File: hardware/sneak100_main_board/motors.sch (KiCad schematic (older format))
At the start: 16 parts, among them J3 Conn_01x06, J4 Conn_01x06, J5 Conn_01x06, J6 Conn_01x06, U1 DRV8835, U2 DRV8835, U3 DRV8835, U4 DRV8835

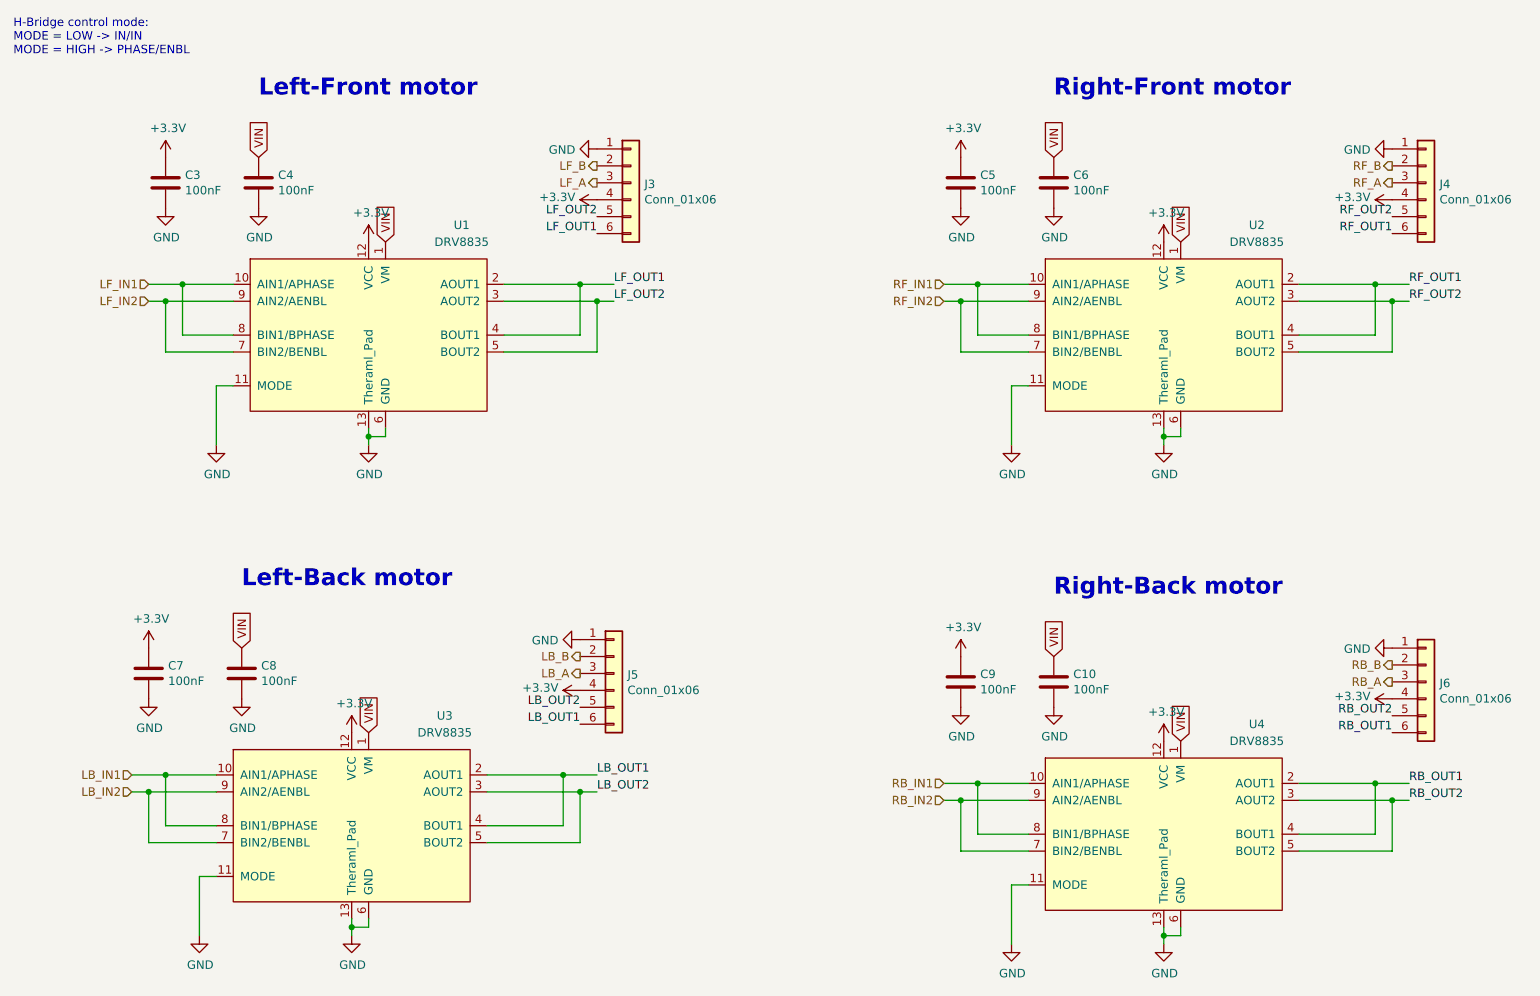
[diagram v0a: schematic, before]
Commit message: Add stm32f405 uC scheme
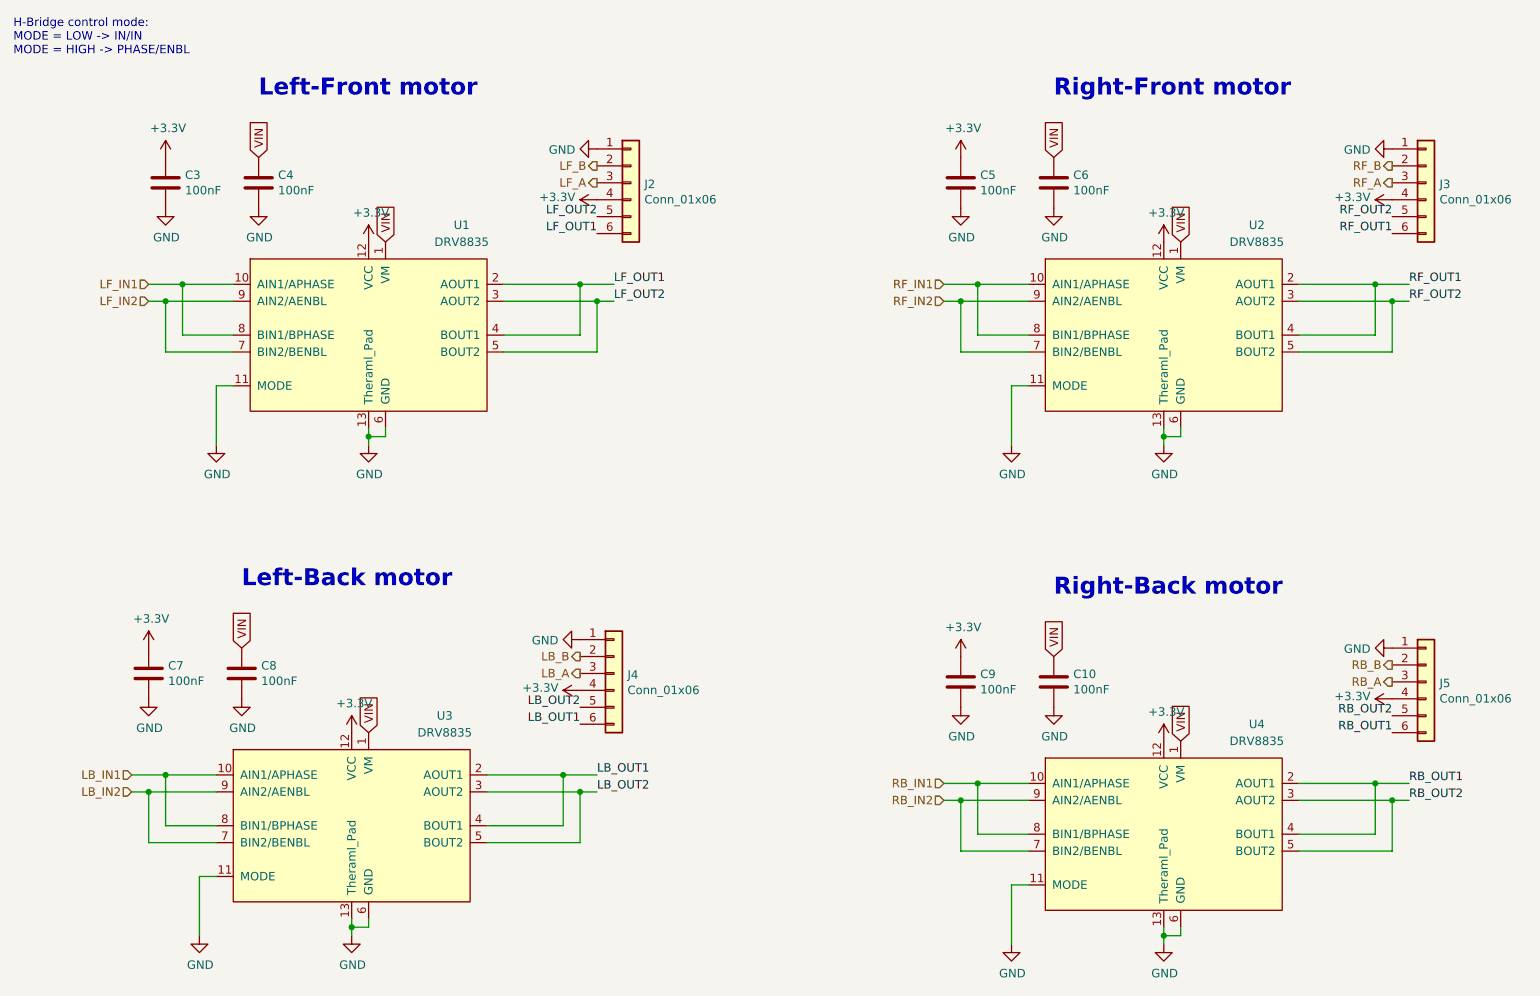
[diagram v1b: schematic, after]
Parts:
- renumbered J3 to J2, J4 to J3, J5 to J4, J6 to J5
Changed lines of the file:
@@
 $Descr A4 11693 8268
 encoding utf-8
-Sheet 4 7
+Sheet 3 7
 Title ""
 Date ""
@@
 Connection ~ 1800 2350
 $Comp
-L Connector_Generic:Conn_01x06 J3
+L Connector_Generic:Conn_01x06 J2
 U 1 1 60E9010F
 P 4550 1650
-F 0 "J3" H 4630 1642 50  0000 L CNN
+F 0 "J2" H 4630 1642 50  0000 L CNN
 F 1 "Conn_01x06" H 4630 1551 50  0000 L CNN
 F 2 "Connector_PinHeader_2.54mm:PinHeader_1x06_P2.54mm_Vertical" H 4550 1650 50  0001 C CNN
@@
 Connection ~ 6500 2350
 $Comp
-L Connector_Generic:Conn_01x06 J4
+L Connector_Generic:Conn_01x06 J3
 U 1 1 60EAF600
 P 9250 1650
-F 0 "J4" H 9330 1642 50  0000 L CNN
+F 0 "J3" H 9330 1642 50  0000 L CNN
 F 1 "Conn_01x06" H 9330 1551 50  0000 L CNN
 F 2 "Connector_PinHeader_2.54mm:PinHeader_1x06_P2.54mm_Vertical" H 9250 1650 50  0001 C CNN
@@
 Connection ~ 1700 5250
 $Comp
-L Connector_Generic:Conn_01x06 J5
+L Connector_Generic:Conn_01x06 J4
 U 1 1 60EB4F56
 P 4450 4550
-F 0 "J5" H 4530 4542 50  0000 L CNN
+F 0 "J4" H 4530 4542 50  0000 L CNN
 F 1 "Conn_01x06" H 4530 4451 50  0000 L CNN
 F 2 "Connector_PinHeader_2.54mm:PinHeader_1x06_P2.54mm_Vertical" H 4450 4550 50  0001 C CNN
@@
 Connection ~ 6500 5300
 $Comp
-L Connector_Generic:Conn_01x06 J6
+L Connector_Generic:Conn_01x06 J5
 U 1 1 60EC1868
 P 9250 4600
-F 0 "J6" H 9330 4592 50  0000 L CNN
+F 0 "J5" H 9330 4592 50  0000 L CNN
 F 1 "Conn_01x06" H 9330 4501 50  0000 L CNN
 F 2 "Connector_PinHeader_2.54mm:PinHeader_1x06_P2.54mm_Vertical" H 9250 4600 50  0001 C CNN

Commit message: Hardware configuration schematic
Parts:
- renumbered C9 to C10, C10 to C11, C3 to C4, C4 to C5, C5 to C6, C6 to C7, C7 to C8, C8 to C9, J2 to J5, J3 to J6, J4 to J7, J5 to J8, U1 to U2, U2 to U3, U3 to U4, U4 to U5

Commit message: Power section scheme
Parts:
- C10, C11, C4, C5, C6, C7, C8, C9: footprint Capacitor_SMD:C_0805_2012Metric -> Capacitor_SMD:C_0603_1608Metric
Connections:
- net VIN renamed SUPPLY
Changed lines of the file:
@@
 F 0 "C4" H 1915 1696 50  0000 L CNN
 F 1 "100nF" H 1915 1605 50  0000 L CNN
-F 2 "Capacitor_SMD:C_0805_2012Metric" H 1838 1500 50  0001 C CNN
+F 2 "Capacitor_SMD:C_0603_1608Metric" H 1838 1500 50  0001 C CNN
 F 3 "~" H 1800 1650 50  0001 C CNN
 	1    1800 1650
@@
 F 0 "C5" H 2465 1696 50  0000 L CNN
 F 1 "100nF" H 2465 1605 50  0000 L CNN
-F 2 "Capacitor_SMD:C_0805_2012Metric" H 2388 1500 50  0001 C CNN
+F 2 "Capacitor_SMD:C_0603_1608Metric" H 2388 1500 50  0001 C CNN
 F 3 "~" H 2350 1650 50  0001 C CNN
 	1    2350 1650
@@
 $EndComp
 Text GLabel 2350 1500 1    50   Input ~ 0
-VIN
-Text GLabel 3100 2000 1    50   Input ~ 0
-VIN
+SUPPLY
 Wire Wire Line
 	3800 2250 4250 2250
@@
 F 0 "C6" H 6615 1696 50  0000 L CNN
 F 1 "100nF" H 6615 1605 50  0000 L CNN
-F 2 "Capacitor_SMD:C_0805_2012Metric" H 6538 1500 50  0001 C CNN
+F 2 "Capacitor_SMD:C_0603_1608Metric" H 6538 1500 50  0001 C CNN
 F 3 "~" H 6500 1650 50  0001 C CNN
 	1    6500 1650
@@
 F 0 "C7" H 7165 1696 50  0000 L CNN
 F 1 "100nF" H 7165 1605 50  0000 L CNN
-F 2 "Capacitor_SMD:C_0805_2012Metric" H 7088 1500 50  0001 C CNN
+F 2 "Capacitor_SMD:C_0603_1608Metric" H 7088 1500 50  0001 C CNN
 F 3 "~" H 7050 1650 50  0001 C CNN
 	1    7050 1650
@@
 	1    0    0    -1
 $EndComp
-Text GLabel 7050 1500 1    50   Input ~ 0
-VIN
-Text GLabel 7800 2000 1    50   Input ~ 0
-VIN
 Wire Wire Line
 	8500 2250 8950 2250
@@
 F 0 "C8" H 1815 4596 50  0000 L CNN
 F 1 "100nF" H 1815 4505 50  0000 L CNN
-F 2 "Capacitor_SMD:C_0805_2012Metric" H 1738 4400 50  0001 C CNN
+F 2 "Capacitor_SMD:C_0603_1608Metric" H 1738 4400 50  0001 C CNN
 F 3 "~" H 1700 4550 50  0001 C CNN
 	1    1700 4550
@@
 F 0 "C9" H 2365 4596 50  0000 L CNN
 F 1 "100nF" H 2365 4505 50  0000 L CNN
-F 2 "Capacitor_SMD:C_0805_2012Metric" H 2288 4400 50  0001 C CNN
+F 2 "Capacitor_SMD:C_0603_1608Metric" H 2288 4400 50  0001 C CNN
 F 3 "~" H 2250 4550 50  0001 C CNN
 	1    2250 4550
@@
 	1    0    0    -1
 $EndComp
-Text GLabel 2250 4400 1    50   Input ~ 0
-VIN
-Text GLabel 3000 4900 1    50   Input ~ 0
-VIN
 Wire Wire Line
 	3700 5150 4150 5150
@@
 F 0 "C10" H 6615 4646 50  0000 L CNN
 F 1 "100nF" H 6615 4555 50  0000 L CNN
-F 2 "Capacitor_SMD:C_0805_2012Metric" H 6538 4450 50  0001 C CNN
+F 2 "Capacitor_SMD:C_0603_1608Metric" H 6538 4450 50  0001 C CNN
 F 3 "~" H 6500 4600 50  0001 C CNN
 	1    6500 4600
@@
 F 0 "C11" H 7165 4646 50  0000 L CNN
 F 1 "100nF" H 7165 4555 50  0000 L CNN
-F 2 "Capacitor_SMD:C_0805_2012Metric" H 7088 4450 50  0001 C CNN
+F 2 "Capacitor_SMD:C_0603_1608Metric" H 7088 4450 50  0001 C CNN
 F 3 "~" H 7050 4600 50  0001 C CNN
 	1    7050 4600
@@
 	1    0    0    -1
 $EndComp
-Text GLabel 7050 4450 1    50   Input ~ 0
-VIN
-Text GLabel 7800 4950 1    50   Input ~ 0
-VIN
 Wire Wire Line
 	8500 5200 8950 5200
@@
 Text HLabel 9050 4500 0    50   Output ~ 0
 RB_B
+Text GLabel 3100 2000 1    50   Input ~ 0
+SUPPLY
+Text GLabel 7800 2000 1    50   Input ~ 0
+SUPPLY
+Text GLabel 7050 1500 1    50   Input ~ 0
+SUPPLY
+Text GLabel 2250 4400 1    50   Input ~ 0
+SUPPLY
+Text GLabel 3000 4900 1    50   Input ~ 0
+SUPPLY
+Text GLabel 7050 4450 1    50   Input ~ 0
+SUPPLY
+Text GLabel 7800 4950 1    50   Input ~ 0
+SUPPLY
 $EndSCHEMATC

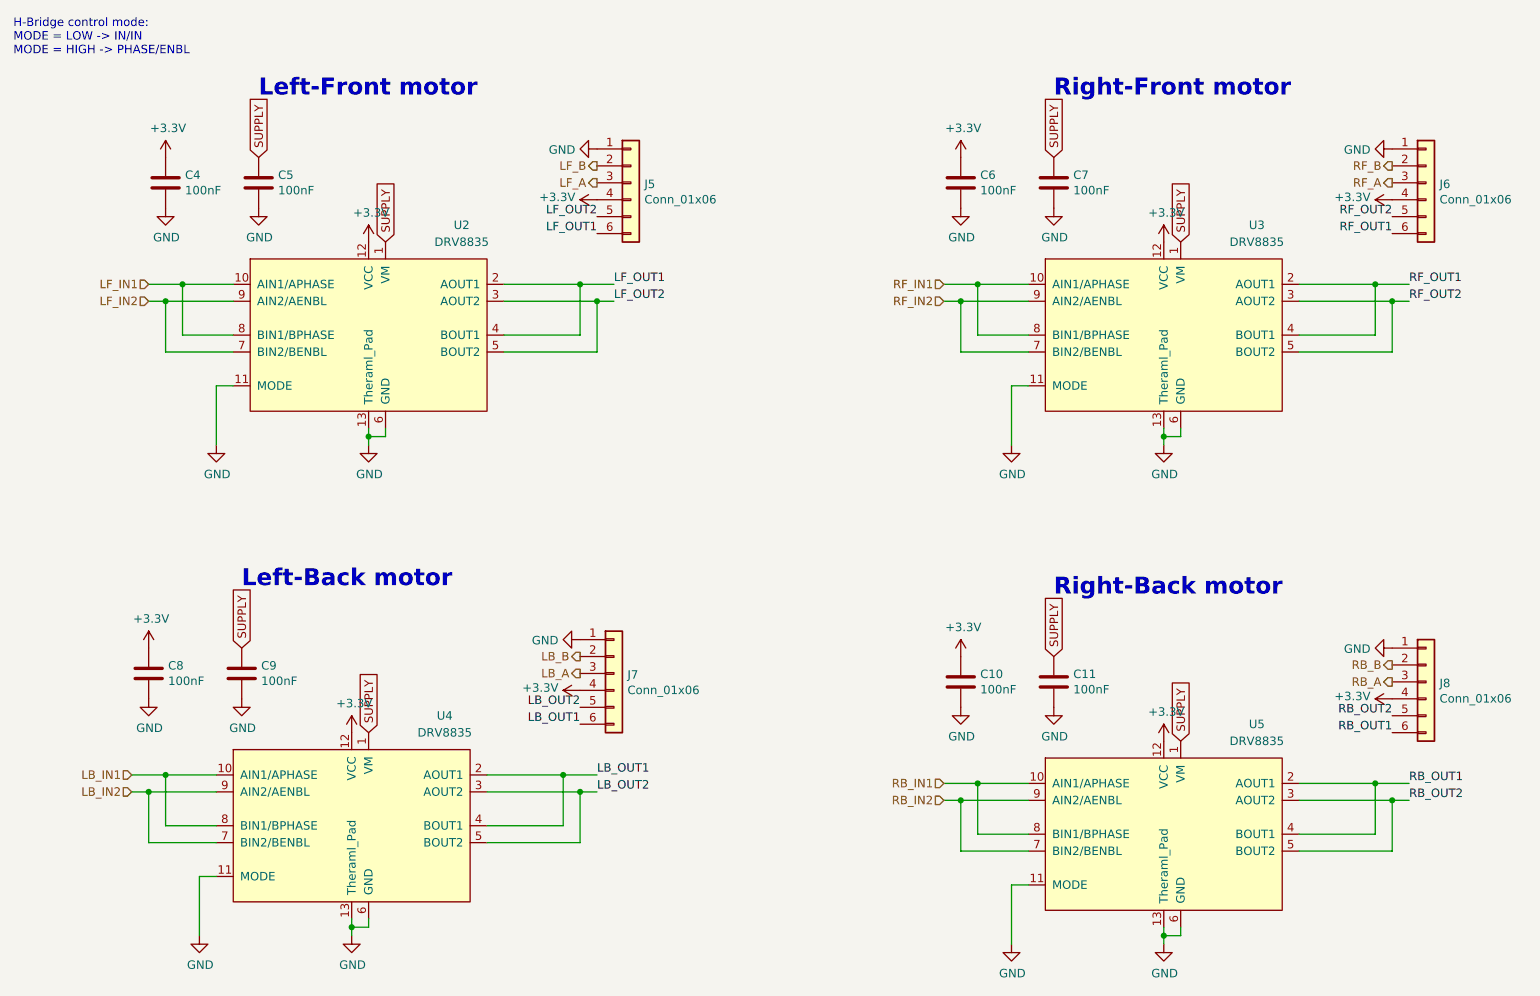
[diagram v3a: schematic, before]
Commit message: USB FDU mode
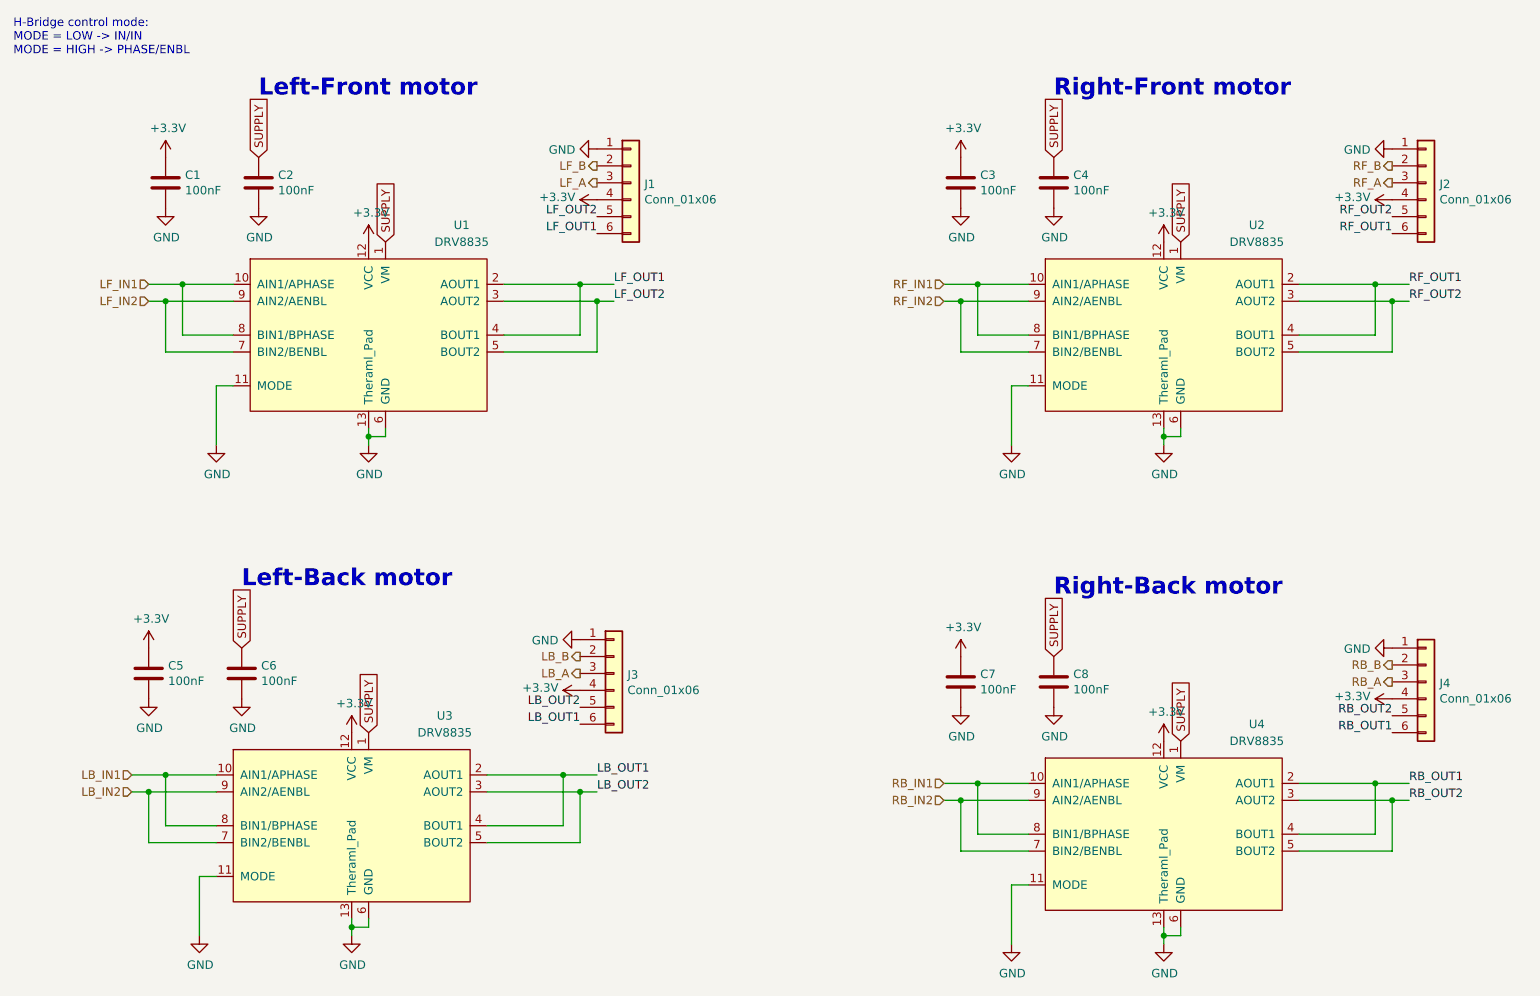
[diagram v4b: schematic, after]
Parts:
- renumbered C4 to C1, C5 to C2, C6 to C3, C7 to C4, C8 to C5, C9 to C6, C10 to C7, C11 to C8, J5 to J1, J6 to J2, J7 to J3, J8 to J4, U2 to U1, U3 to U2, U4 to U3, U5 to U4

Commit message: Layout progress
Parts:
- J1, J2, J3, J4: footprint Connector_PinHeader_2.54mm:PinHeader_1x06_P2.54mm_Vertical -> Connector_JST:JST_PH_S6B-PH-K_1x06_P2.00mm_Horizontal
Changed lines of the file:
@@
 F 0 "J1" H 4630 1642 50  0000 L CNN
 F 1 "Conn_01x06" H 4630 1551 50  0000 L CNN
-F 2 "Connector_PinHeader_2.54mm:PinHeader_1x06_P2.54mm_Vertical" H 4550 1650 50  0001 C CNN
+F 2 "Connector_JST:JST_PH_S6B-PH-K_1x06_P2.00mm_Horizontal" H 4550 1650 50  0001 C CNN
 F 3 "~" H 4550 1650 50  0001 C CNN
 	1    4550 1650
@@
 F 0 "J2" H 9330 1642 50  0000 L CNN
 F 1 "Conn_01x06" H 9330 1551 50  0000 L CNN
-F 2 "Connector_PinHeader_2.54mm:PinHeader_1x06_P2.54mm_Vertical" H 9250 1650 50  0001 C CNN
+F 2 "Connector_JST:JST_PH_S6B-PH-K_1x06_P2.00mm_Horizontal" H 9250 1650 50  0001 C CNN
 F 3 "~" H 9250 1650 50  0001 C CNN
 	1    9250 1650
@@
 F 0 "J3" H 4530 4542 50  0000 L CNN
 F 1 "Conn_01x06" H 4530 4451 50  0000 L CNN
-F 2 "Connector_PinHeader_2.54mm:PinHeader_1x06_P2.54mm_Vertical" H 4450 4550 50  0001 C CNN
+F 2 "Connector_JST:JST_PH_S6B-PH-K_1x06_P2.00mm_Horizontal" H 4450 4550 50  0001 C CNN
 F 3 "~" H 4450 4550 50  0001 C CNN
 	1    4450 4550
@@
 F 0 "J4" H 9330 4592 50  0000 L CNN
 F 1 "Conn_01x06" H 9330 4501 50  0000 L CNN
-F 2 "Connector_PinHeader_2.54mm:PinHeader_1x06_P2.54mm_Vertical" H 9250 4600 50  0001 C CNN
+F 2 "Connector_JST:JST_PH_S6B-PH-K_1x06_P2.00mm_Horizontal" H 9250 4600 50  0001 C CNN
 F 3 "~" H 9250 4600 50  0001 C CNN
 	1    9250 4600
